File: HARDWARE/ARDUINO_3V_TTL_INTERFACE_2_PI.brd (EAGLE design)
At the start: 74.9 x 57.1 mm, 41 parts, among them J1 RASPBERRYPI-40-PIN-GPIO_SMT, Q1 BCM857BS, Q2 DMG2305UX, U1 ATMEGA328P, Y1 8MHz

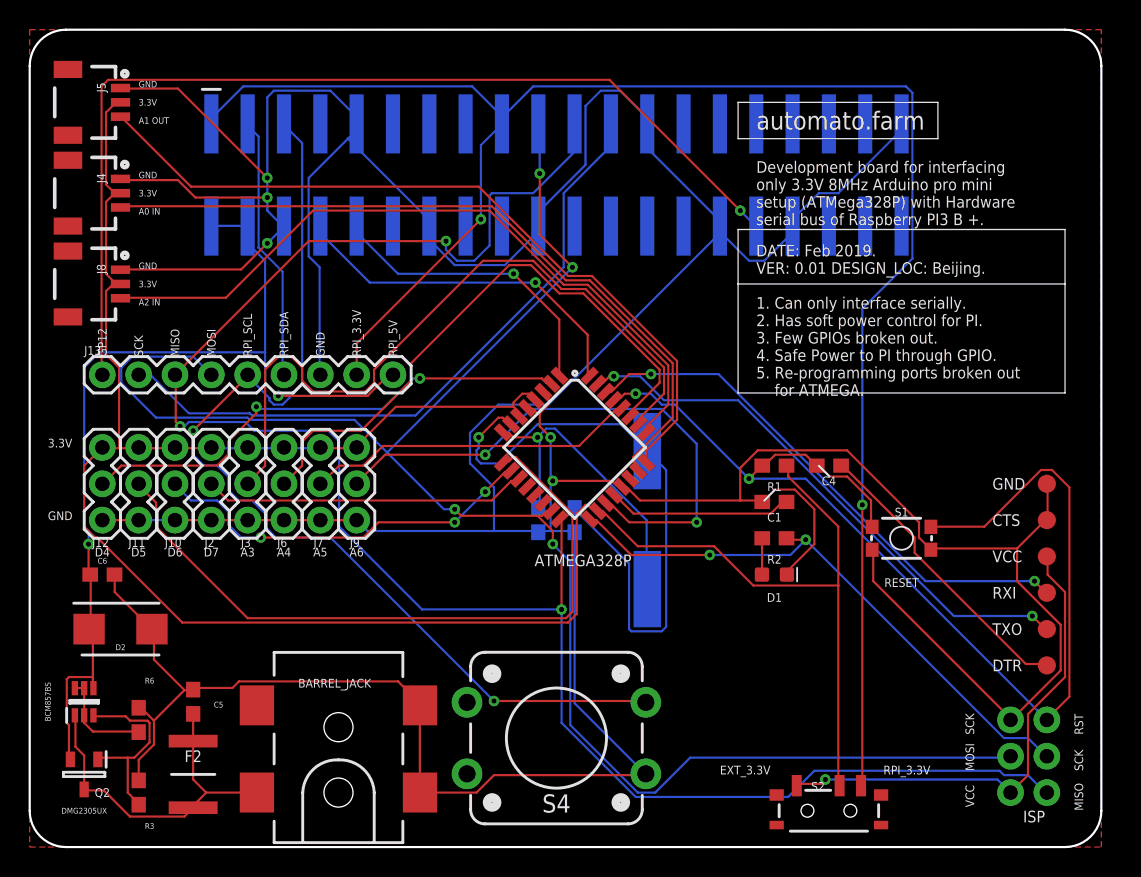
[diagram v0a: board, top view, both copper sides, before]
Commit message: added a jumper to separate ext voltage for testing it the volt reg citcuit doesn't work
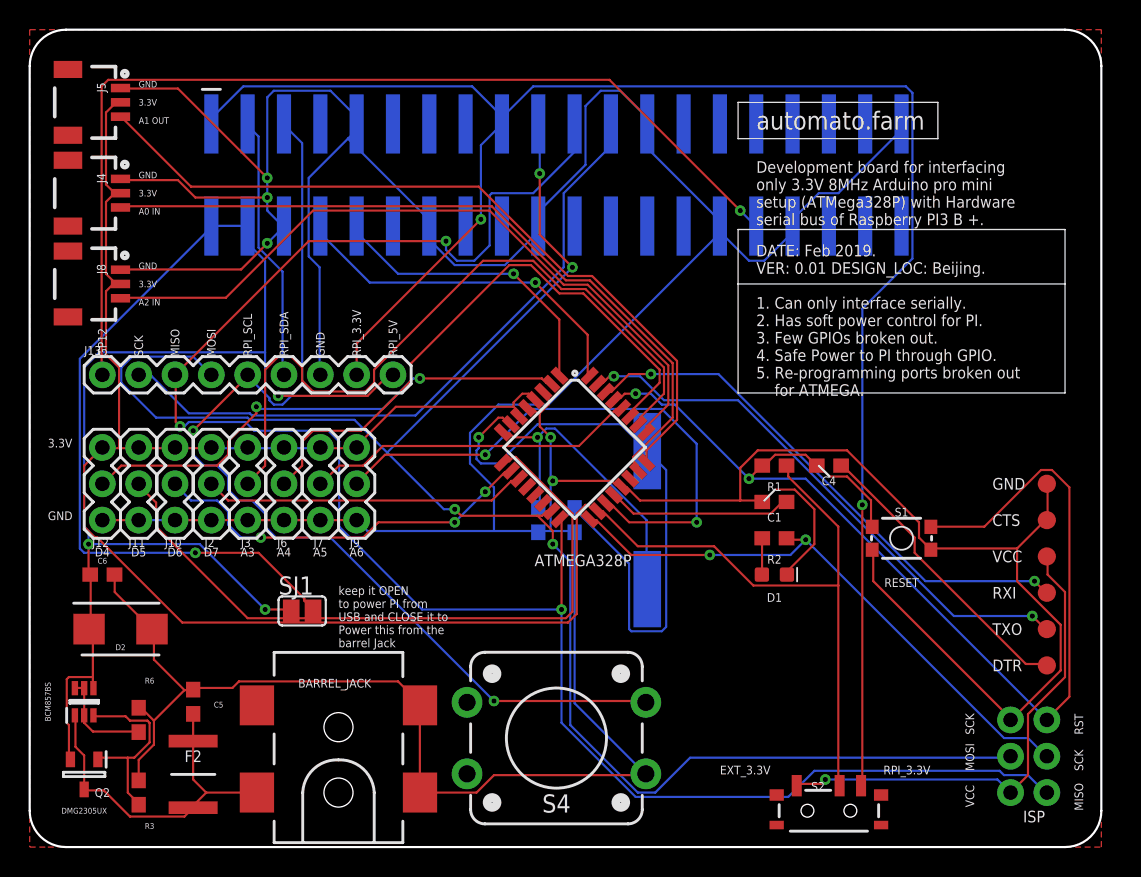
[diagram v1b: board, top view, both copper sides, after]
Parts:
- added SJ1: (no value), jumper:SJ
- D1: value GREEN -> RED
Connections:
- new net N$2: J1.2, J1.4, SJ1.2
- net RPI_5V: now also SJ1.1; no longer J1.2, J1.4
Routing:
- net N$2: track 0.00 -> 47.2 mm, vias 0 -> 1
- net RPI_5V: track 67.5 -> 80.0 mm, vias 2 -> 3
- net RESET: track 80.0 -> 81.1 mm
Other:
- board text added: "keep it OPEN to power PI from USB and CLOSE it to Power this from the barrel Jack"
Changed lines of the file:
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@@
 <wire x1="51.3588" y1="24.2316" x2="52.1208" y2="24.9936" width="0.1524" layer="21"/>
 <wire x1="55.1688" y1="26.67" x2="55.9308" y2="25.908" width="0.1524" layer="21"/>
+<text x="21.59" y="13.97" size="0.6096" layer="21" font="fixed">keep it OPEN
+to power PI from
+USB and CLOSE it to
+Power this from the
+barrel Jack</text>
 </plain>
 <attributes>
@@
 <attribute name="VALUE" x="70.485" y="22.098" size="0.0254" layer="27"/>
 </element>
-<element name="D1" library="SparkFun-LED" library_urn="urn:adsk.eagle:library:529" package="LED-0603" package3d_urn="urn:adsk.eagle:package:39354/1" value="GREEN" x="52.07" y="19.05" smashed="yes">
+<element name="D1" library="SparkFun-LED" library_urn="urn:adsk.eagle:library:529" package="LED-0603" package3d_urn="urn:adsk.eagle:package:39354/1" value="RED" x="52.07" y="19.05" smashed="yes">
 <attribute name="NAME" x="52.07" y="17.145" size="0.6096" layer="21" font="fixed" ratio="20" align="bottom-center"/>
 <attribute name="PROD_ID" value="DIO-00821" x="67.31" y="-83.82" size="1.778" layer="27" display="off"/>
@@
 <attribute name="PROD_ID" value="XTAL-11706" x="-22.86" y="64.77" size="1.778" layer="28" rot="MR90" display="off"/>
 <attribute name="VALUE" x="40.513" y="22.86" size="0.6096" layer="28" font="vector" ratio="20" rot="MR90" align="top-center"/>
+</element>
+<element name="SJ1" library="jumper" library_urn="urn:adsk.eagle:library:252" package="SJ" package3d_urn="urn:adsk.eagle:package:15471/1" value="" x="19.05" y="16.51" smashed="yes">
+<attribute name="NAME" x="17.399" y="17.653" size="1.27" layer="25" ratio="10"/>
+<attribute name="VALUE" x="19.4501" y="16.51" size="0.02" layer="27"/>
 </element>
 </elements>
@@
 </signal>
 <signal name="RPI_5V">
-<contactref element="J1" pad="2"/>
-<contactref element="J1" pad="4"/>
 <contactref element="Q2" pad="2"/>
 <contactref element="Q1" pad="4"/>
@@
 <wire x1="16.4592" y1="34.5948" x2="16.4592" y2="32.4612" width="0.1524" layer="16"/>
 <wire x1="15.24" y1="42.2148" x2="16.4592" y2="40.9956" width="0.1524" layer="16"/>
-<wire x1="15.24" y1="43.4213" x2="15.24" y2="42.2148" width="0.1524" layer="16"/>
 <wire x1="25.2984" y1="32.9184" x2="25.4" y2="33.02" width="0.1524" layer="1"/>
-<wire x1="15.24" y1="43.434" x2="12.8016" y2="43.434" width="0.1524" layer="16"/>
-<wire x1="12.8016" y1="43.434" x2="12.7" y2="43.4213" width="0.1524" layer="16"/>
-<wire x1="15.24" y1="43.434" x2="15.24" y2="43.4213" width="0.1524" layer="16"/>
 <wire x1="4.1148" y1="21.1836" x2="4.1148" y2="19.05" width="0.1524" layer="1"/>
 <wire x1="4.1148" y1="22.098" x2="4.1148" y2="21.1836" width="0.1524" layer="16"/>
@@
 <via x="17.3736" y="31.5468" extent="1-16" drill="0.35"/>
 <via x="4.1148" y="21.1836" extent="1-16" drill="0.35"/>
+<contactref element="SJ1" pad="1"/>
+<wire x1="16.4592" y1="16.6116" x2="18.288" y2="16.6116" width="0.1524" layer="1"/>
+<wire x1="11.8872" y1="21.1836" x2="16.4592" y2="16.6116" width="0.1524" layer="16"/>
+<wire x1="4.1148" y1="21.1836" x2="11.8872" y2="21.1836" width="0.1524" layer="16"/>
+<wire x1="18.288" y1="16.6116" x2="18.288" y2="16.51" width="0.1524" layer="1"/>
+<via x="16.4592" y="16.6116" extent="1-16" drill="0.35"/>
 </signal>
 <signal name="V_REG">
@@
 <wire x1="55.9308" y1="25.908" x2="57.15" y2="25.908" width="0.1524" layer="1"/>
 <wire x1="58.8264" y1="22.4028" x2="58.91" y2="22.39" width="0.1524" layer="1"/>
-<wire x1="55.1688" y1="26.67" x2="55.03" y2="26.67" width="0.1524" layer="1"/>
 <wire x1="52.1208" y1="27.432" x2="51.3588" y2="26.67" width="0.1524" layer="1"/>
 <wire x1="54.2544" y1="27.432" x2="52.1208" y2="27.432" width="0.1524" layer="1"/>
@@
 <via x="42.3672" y="31.6992" extent="1-16" drill="0.35"/>
 <via x="50.292" y="25.7556" extent="1-16" drill="0.35"/>
+<wire x1="55.1688" y1="26.67" x2="55.9308" y2="25.908" width="0.1524" layer="1"/>
+<wire x1="55.1688" y1="26.67" x2="55.03" y2="26.67" width="0.1524" layer="1"/>
 </signal>
 <signal name="DTR">
@@
 <via x="49.6824" y="44.5008" extent="1-16" drill="0.35"/>
 </signal>
+<signal name="N$2">
+<contactref element="J1" pad="4"/>
+<contactref element="J1" pad="2"/>
+<contactref element="SJ1" pad="2"/>
+<wire x1="19.2024" y1="17.2212" x2="19.812" y2="16.6116" width="0.1524" layer="1"/>
+<wire x1="19.2024" y1="17.3736" x2="19.2024" y2="17.2212" width="0.1524" layer="1"/>
+<wire x1="16.002" y1="20.574" x2="19.2024" y2="17.3736" width="0.1524" layer="1"/>
+<wire x1="11.5824" y1="20.574" x2="16.002" y2="20.574" width="0.1524" layer="1"/>
+<wire x1="3.81" y1="20.574" x2="11.5824" y2="20.574" width="0.1524" layer="16"/>
+<wire x1="3.5052" y1="20.8788" x2="3.81" y2="20.574" width="0.1524" layer="16"/>
+<wire x1="3.5052" y1="34.1376" x2="3.5052" y2="20.8788" width="0.1524" layer="16"/>
+<wire x1="12.6492" y1="43.2816" x2="3.5052" y2="34.1376" width="0.1524" layer="16"/>
+<wire x1="19.812" y1="16.6116" x2="19.812" y2="16.51" width="0.1524" layer="1"/>
+<wire x1="12.6492" y1="43.2816" x2="12.7" y2="43.4213" width="0.1524" layer="16"/>
+<wire x1="12.8016" y1="43.434" x2="15.24" y2="43.434" width="0.1524" layer="16"/>
+<wire x1="15.24" y1="43.434" x2="15.24" y2="43.4213" width="0.1524" layer="16"/>
+<wire x1="12.8016" y1="43.434" x2="12.7" y2="43.4213" width="0.1524" layer="16"/>
+<via x="11.5824" y="20.574" extent="1-16" drill="0.35"/>
+</signal>
 </signals>
